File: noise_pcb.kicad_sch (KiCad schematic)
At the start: 29 parts, among them J101 PINK_OUT, J102 WHITE_OUT, J103 FILT_WHITE, J104 INV_FILT_WHITE, U1 TL072, U3 ElectricDruid_Noise2, U4 TL072

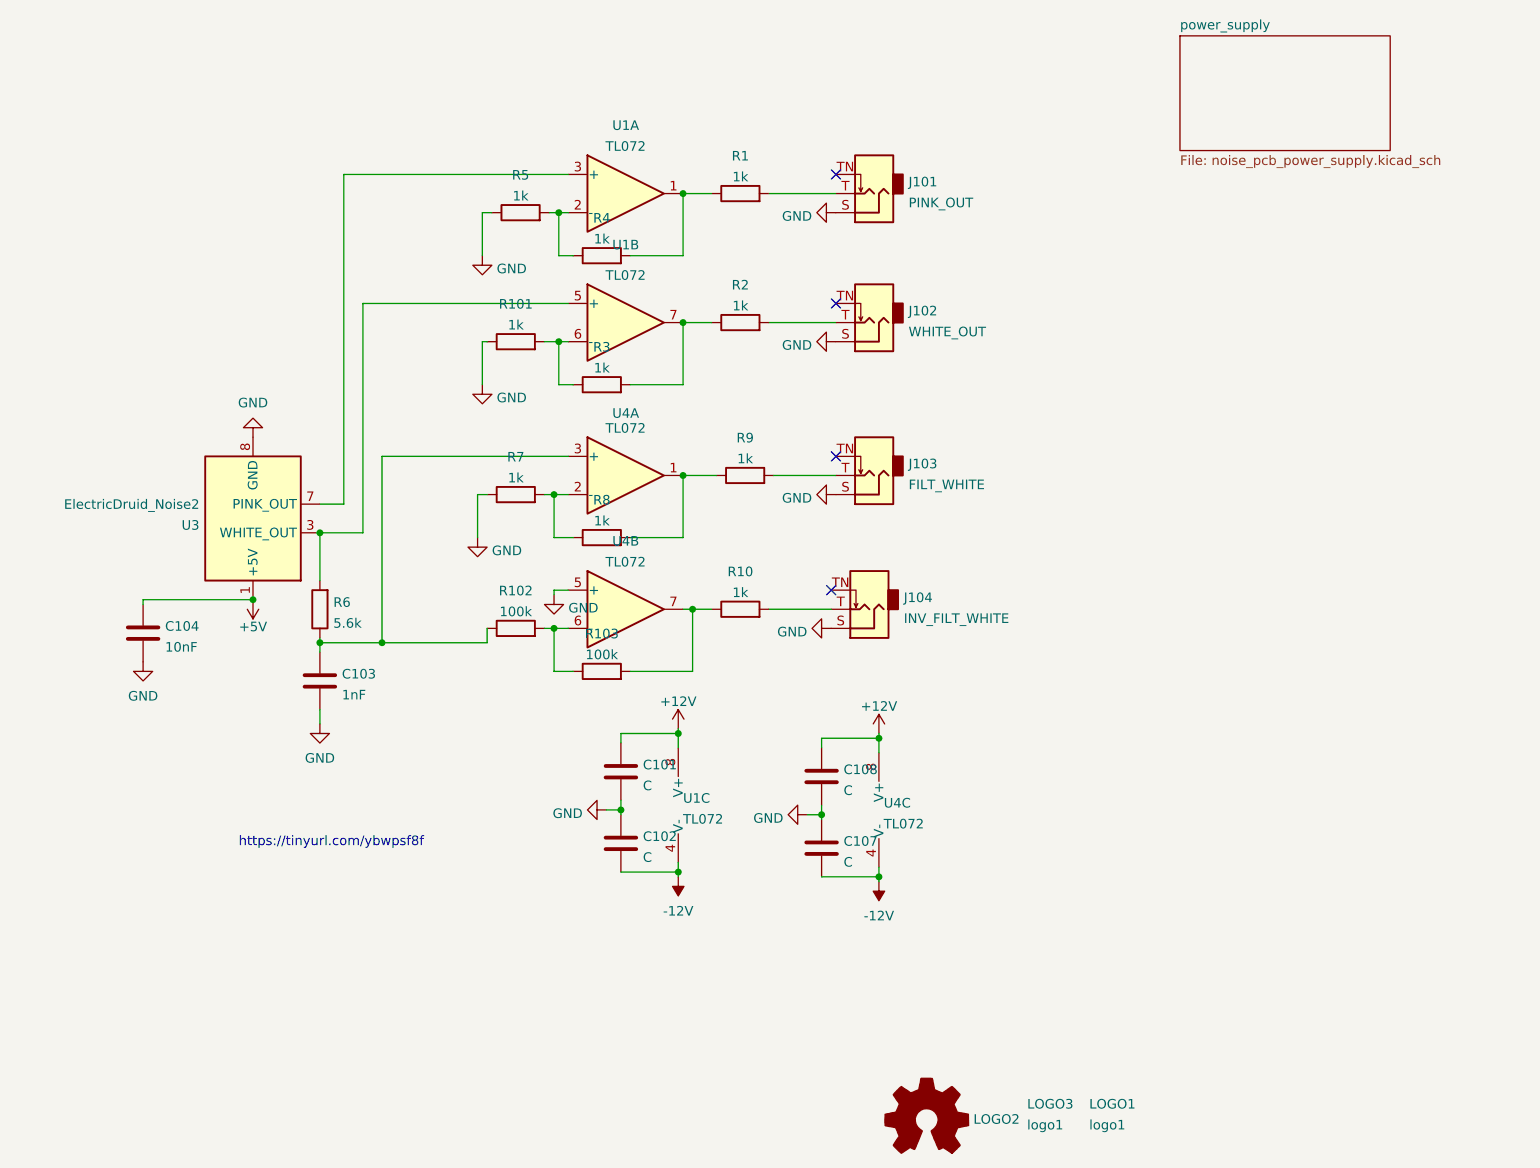
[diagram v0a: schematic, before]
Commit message: Assembly notes, value fixes, README
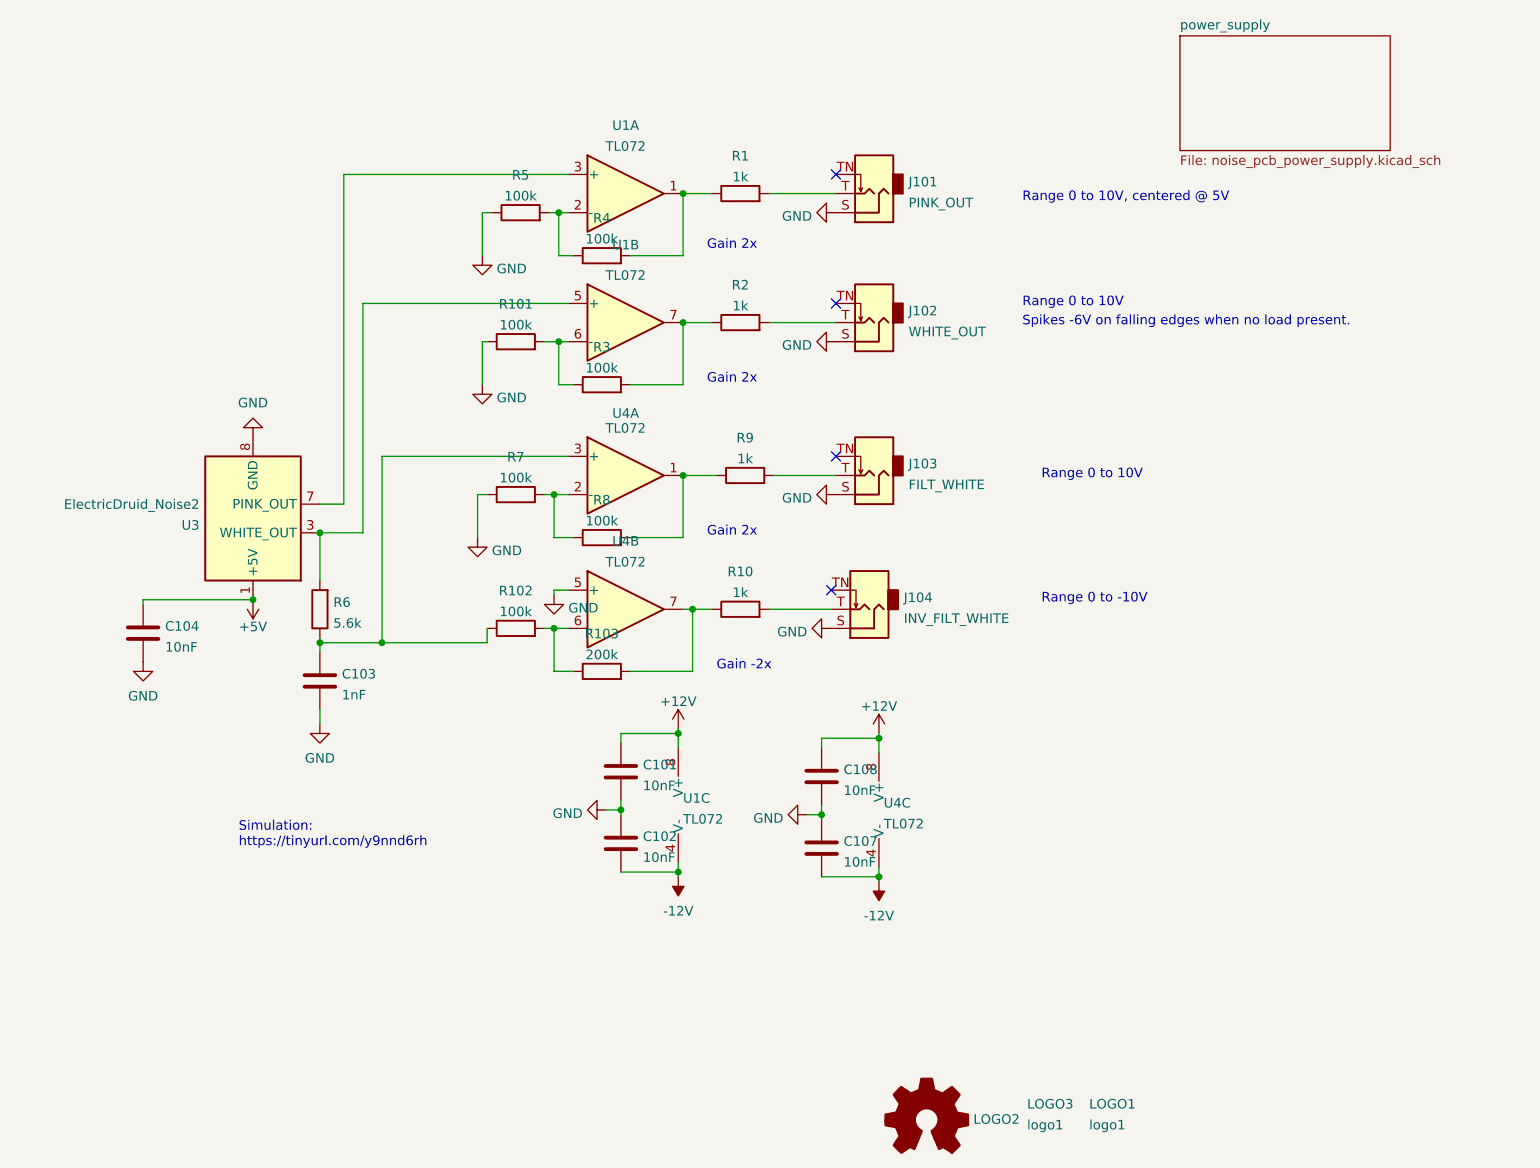
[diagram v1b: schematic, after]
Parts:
- C101, C102, C107, C108: value C -> 10nF
- R101, R3, R4, R5, R7, R8: value 1k -> 100k
- R103: value 100k -> 200k
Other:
- note added: "Gain -2x"
- note added: "Gain 2x"
- note added: "Range 0 to -10V"
- note added: "Range 0 to 10V"
- note added: "Range 0 to 10V, centered @ 5V"
- note added: "Simulation: https://tinyurl.com/y9nnd6rh"
- note added: "Spikes -6V on falling edges when no load present."
- note removed: "https://tinyurl.com/ybwpsf8f"
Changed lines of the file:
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@@
     (stroke (width 0) (type default) (color 0 0 0 0))
   )
-  (text "https://tinyurl.com/ybwpsf8f" (at 92.71 137.795 0)
+  (text "Gain -2x" (at 156.21 114.3 0)
+    (effects (font (size 1.27 1.27)) (justify left bottom))
+  )
+  (text "Range 0 to 10V, centered @ 5V" (at 196.85 52.07 0)
+    (effects (font (size 1.27 1.27)) (justify left bottom))
+  )
+  (text "Gain 2x" (at 154.94 76.2 0)
+    (effects (font (size 1.27 1.27)) (justify left bottom))
+  )
+  (text "Gain 2x" (at 154.94 58.42 0)
+    (effects (font (size 1.27 1.27)) (justify left bottom))
+  )
+  (text "Range 0 to 10V" (at 199.39 88.9 0)
+    (effects (font (size 1.27 1.27)) (justify left bottom))
+  )
+  (text "Simulation:\nhttps://tinyurl.com/y9nnd6rh" (at 92.71 137.795 0)
+    (effects (font (size 1.27 1.27)) (justify left bottom))
+  )
+  (text "Range 0 to -10V" (at 199.39 105.41 0)
+    (effects (font (size 1.27 1.27)) (justify left bottom))
+  )
+  (text "Spikes -6V on falling edges when no load present." (at 196.85 68.58 0)
+    (effects (font (size 1.27 1.27)) (justify left bottom))
+  )
+  (text "Range 0 to 10V" (at 196.85 66.04 0)
+    (effects (font (size 1.27 1.27)) (justify left bottom))
+  )
+  (text "Gain 2x" (at 154.94 96.52 0)
     (effects (font (size 1.27 1.27)) (justify left bottom))
   )
@@
       (effects (font (size 1.27 1.27)) (justify left))
     )
-    (property "Value" "C" (id 1) (at 173.101 139.6616 0)
+    (property "Value" "10nF" (id 1) (at 173.101 139.6616 0)
       (effects (font (size 1.27 1.27)) (justify left))
     )
@@
       (effects (font (size 1.27 1.27)) (justify left))
     )
-    (property "Value" "C" (id 1) (at 146.431 129.5016 0)
+    (property "Value" "10nF" (id 1) (at 146.431 129.5016 0)
       (effects (font (size 1.27 1.27)) (justify left))
     )
@@
       (effects (font (size 1.27 1.27)) (justify left))
     )
-    (property "Value" "C" (id 1) (at 146.431 139.0266 0)
+    (property "Value" "10nF" (id 1) (at 146.431 139.0266 0)
       (effects (font (size 1.27 1.27)) (justify left))
     )
@@
     (in_bom yes) (on_board yes) (fields_autoplaced)
     (property "Reference" "R4" (id 0) (at 140.97 54.0725 90))
-    (property "Value" "1k" (id 1) (at 140.97 56.8476 90))
+    (property "Value" "100k" (id 1) (at 140.97 56.8476 90))
     (property "Footprint" "Resistor_SMD:R_1206_3216Metric_Pad1.30x1.75mm_HandSolder" (id 2) (at 140.97 60.833 90)
       (effects (font (size 1.27 1.27)) hide)
@@
     (in_bom yes) (on_board yes) (fields_autoplaced)
     (property "Reference" "R5" (id 0) (at 130.175 48.3575 90))
-    (property "Value" "1k" (id 1) (at 130.175 51.1326 90))
+    (property "Value" "100k" (id 1) (at 130.175 51.1326 90))
     (property "Footprint" "Resistor_SMD:R_1206_3216Metric_Pad1.30x1.75mm_HandSolder" (id 2) (at 130.175 55.118 90)
       (effects (font (size 1.27 1.27)) hide)
@@
     (in_bom yes) (on_board yes)
     (property "Reference" "R8" (id 0) (at 140.97 91.5375 90))
-    (property "Value" "1k" (id 1) (at 140.97 94.3126 90))
+    (property "Value" "100k" (id 1) (at 140.97 94.3126 90))
     (property "Footprint" "Resistor_SMD:R_1206_3216Metric_Pad1.30x1.75mm_HandSolder" (id 2) (at 140.97 98.298 90)
       (effects (font (size 1.27 1.27)) hide)
@@
     (in_bom yes) (on_board yes) (fields_autoplaced)
     (property "Reference" "R101" (id 0) (at 129.54 65.5025 90))
-    (property "Value" "1k" (id 1) (at 129.54 68.2776 90))
+    (property "Value" "100k" (id 1) (at 129.54 68.2776 90))
     (property "Footprint" "Resistor_SMD:R_1206_3216Metric_Pad1.30x1.75mm_HandSolder" (id 2) (at 129.54 72.263 90)
       (effects (font (size 1.27 1.27)) hide)
@@
     (in_bom yes) (on_board yes) (fields_autoplaced)
     (property "Reference" "R7" (id 0) (at 129.54 85.8225 90))
-    (property "Value" "1k" (id 1) (at 129.54 88.5976 90))
+    (property "Value" "100k" (id 1) (at 129.54 88.5976 90))
     (property "Footprint" "Resistor_SMD:R_1206_3216Metric_Pad1.30x1.75mm_HandSolder" (id 2) (at 129.54 92.583 90)
       (effects (font (size 1.27 1.27)) hide)
@@
     (in_bom yes) (on_board yes) (fields_autoplaced)
     (property "Reference" "R3" (id 0) (at 140.97 71.2175 90))
-    (property "Value" "1k" (id 1) (at 140.97 73.9926 90))
+    (property "Value" "100k" (id 1) (at 140.97 73.9926 90))
     (property "Footprint" "Resistor_SMD:R_1206_3216Metric_Pad1.30x1.75mm_HandSolder" (id 2) (at 140.97 77.978 90)
       (effects (font (size 1.27 1.27)) hide)
@@
     (in_bom yes) (on_board yes)
     (property "Reference" "R103" (id 0) (at 140.97 109.3175 90))
-    (property "Value" "100k" (id 1) (at 140.97 112.0926 90))
+    (property "Value" "200k" (id 1) (at 140.97 112.0926 90))
     (property "Footprint" "Resistor_SMD:R_1206_3216Metric_Pad1.30x1.75mm_HandSolder" (id 2) (at 140.97 116.078 90)
       (effects (font (size 1.27 1.27)) hide)
@@
       (effects (font (size 1.27 1.27)) (justify left))
     )
-    (property "Value" "C" (id 1) (at 173.101 130.1366 0)
+    (property "Value" "10nF" (id 1) (at 173.101 130.1366 0)
       (effects (font (size 1.27 1.27)) (justify left))
     )
@@
     )
     (path "/6a71deaf-8ed8-4b4e-a097-04761c3a9b7b"
-      (reference "C101") (unit 1) (value "C") (footprint "Capacitor_THT:C_Disc_D6.0mm_W4.4mm_P5.00mm")
+      (reference "C101") (unit 1) (value "10nF") (footprint "Capacitor_THT:C_Disc_D6.0mm_W4.4mm_P5.00mm")
     )
     (path "/6b96e9a1-e255-499a-aa20-f60ecd5d6955"
-      (reference "C102") (unit 1) (value "C") (footprint "Capacitor_THT:C_Disc_D6.0mm_W4.4mm_P5.00mm")
+      (reference "C102") (unit 1) (value "10nF") (footprint "Capacitor_THT:C_Disc_D6.0mm_W4.4mm_P5.00mm")
     )
     (path "/8f5ce17a-fae1-470f-a98d-221b0e94565d"
@@
     )
     (path "/2ed1b884-98f0-400f-97e6-6e1445d7a0b8"
-      (reference "C107") (unit 1) (value "C") (footprint "Capacitor_THT:C_Disc_D6.0mm_W4.4mm_P5.00mm")
+      (reference "C107") (unit 1) (value "10nF") (footprint "Capacitor_THT:C_Disc_D6.0mm_W4.4mm_P5.00mm")
     )
     (path "/ffb095dd-5623-4b48-97b7-581bd252c9b2"
-      (reference "C108") (unit 1) (value "C") (footprint "Capacitor_THT:C_Disc_D6.0mm_W4.4mm_P5.00mm")
+      (reference "C108") (unit 1) (value "10nF") (footprint "Capacitor_THT:C_Disc_D6.0mm_W4.4mm_P5.00mm")
     )
     (path "/c045b4c2-7302-48c5-b137-d1ad353be048/05c022a7-f9f5-45a3-9346-213e8fce81d3"
@@
     )
     (path "/ae4abfc0-c74f-4aca-ac2d-a9ea6aacaaaf"
-      (reference "R3") (unit 1) (value "1k") (footprint "Resistor_SMD:R_1206_3216Metric_Pad1.30x1.75mm_HandSolder")
+      (reference "R3") (unit 1) (value "100k") (footprint "Resistor_SMD:R_1206_3216Metric_Pad1.30x1.75mm_HandSolder")
     )
     (path "/796365eb-3b00-481a-b3b0-b83241f40275"
-      (reference "R4") (unit 1) (value "1k") (footprint "Resistor_SMD:R_1206_3216Metric_Pad1.30x1.75mm_HandSolder")
+      (reference "R4") (unit 1) (value "100k") (footprint "Resistor_SMD:R_1206_3216Metric_Pad1.30x1.75mm_HandSolder")
     )
     (path "/8134c256-d4c7-4a69-b994-3108ed996f95"
-      (reference "R5") (unit 1) (value "1k") (footprint "Resistor_SMD:R_1206_3216Metric_Pad1.30x1.75mm_HandSolder")
+      (reference "R5") (unit 1) (value "100k") (footprint "Resistor_SMD:R_1206_3216Metric_Pad1.30x1.75mm_HandSolder")
     )
     (path "/0bee5d4c-0b61-4267-a49e-f88f005cf8b6"
@@
     )
     (path "/abd560d3-acc2-4742-b462-be0765f942b5"
-      (reference "R7") (unit 1) (value "1k") (footprint "Resistor_SMD:R_1206_3216Metric_Pad1.30x1.75mm_HandSolder")
+      (reference "R7") (unit 1) (value "100k") (footprint "Resistor_SMD:R_1206_3216Metric_Pad1.30x1.75mm_HandSolder")
     )
     (path "/8adab083-05b5-4a52-9cab-e1546510f4c1"
-      (reference "R8") (unit 1) (value "1k") (footprint "Resistor_SMD:R_1206_3216Metric_Pad1.30x1.75mm_HandSolder")
+      (reference "R8") (unit 1) (value "100k") (footprint "Resistor_SMD:R_1206_3216Metric_Pad1.30x1.75mm_HandSolder")
     )
     (path "/6b55610a-a6bb-470f-b556-b39436ab4bbf"
@@
     )
     (path "/8fd95ddc-a582-497f-8905-973e937da1a0"
-      (reference "R101") (unit 1) (value "1k") (footprint "Resistor_SMD:R_1206_3216Metric_Pad1.30x1.75mm_HandSolder")
+      (reference "R101") (unit 1) (value "100k") (footprint "Resistor_SMD:R_1206_3216Metric_Pad1.30x1.75mm_HandSolder")
     )
     (path "/f4aefe93-5b2d-431f-8bb1-6afb22325813"
@@
     )
     (path "/ef7ff756-d2a6-4ae0-8373-5dceb07e0d02"
-      (reference "R103") (unit 1) (value "100k") (footprint "Resistor_SMD:R_1206_3216Metric_Pad1.30x1.75mm_HandSolder")
+      (reference "R103") (unit 1) (value "200k") (footprint "Resistor_SMD:R_1206_3216Metric_Pad1.30x1.75mm_HandSolder")
     )
     (path "/2b3b289c-9356-4727-acba-91ef9abb00ec"

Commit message: Title block updates and pdf
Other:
- company: (none) -> Robot Dialogs
- title: noise_pcb -> Noise PCB
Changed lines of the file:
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@@
   (paper "A4")
   (title_block
-    (title "noise_pcb")
+    (title "Noise PCB")
     (date "2022-01-31")
-    (rev "v1")
+    (rev "1.0")
+    (company "Robot Dialogs")
   )
   (junction (at 134.62 108.585) (diameter 0) (color 0 0 0 0)
@@
     (pin "1")
   )
-  (symbol (lib_id "My Stuff:logo1") (at 205.105 172.72 0) (unit 1)
-    (in_bom yes) (on_board yes) (fields_autoplaced)
-    (property "Reference" "LOGO1" (id 0) (at 205.74 171.8115 0)
-      (effects (font (size 1.27 1.27)) (justify left))
-    )
-    (property "Value" "logo1" (id 1) (at 205.74 174.5866 0)
-      (effects (font (size 1.27 1.27)) (justify left))
-    )
-    (property "Footprint" "My Stuff:Logo2" (id 2) (at 205.105 171.45 0)
-      (effects (font (size 1.27 1.27)) hide)
-    )
-    (property "Datasheet" "" (id 3) (at 205.105 171.45 0)
+  (symbol (lib_id "My Stuff:logo1") (at 220.98 172.085 0) (unit 1)
+    (in_bom yes) (on_board yes) (fields_autoplaced)
+    (property "Reference" "LOGO1" (id 0) (at 221.615 171.1765 0)
+      (effects (font (size 1.27 1.27)) (justify left))
+    )
+    (property "Value" "logo1" (id 1) (at 221.615 173.9516 0)
+      (effects (font (size 1.27 1.27)) (justify left))
+    )
+    (property "Footprint" "My Stuff:Logo2" (id 2) (at 220.98 170.815 0)
+      (effects (font (size 1.27 1.27)) hide)
+    )
+    (property "Datasheet" "" (id 3) (at 220.98 170.815 0)
       (effects (font (size 1.27 1.27)) hide)
     )
@@
     (pin "2")
   )
-  (symbol (lib_id "My Stuff:logo1") (at 196.85 172.72 0) (unit 1)
-    (in_bom yes) (on_board yes) (fields_autoplaced)
-    (property "Reference" "LOGO3" (id 0) (at 197.485 171.8115 0)
-      (effects (font (size 1.27 1.27)) (justify left))
-    )
-    (property "Value" "logo1" (id 1) (at 197.485 174.5866 0)
-      (effects (font (size 1.27 1.27)) (justify left))
-    )
-    (property "Footprint" "My Stuff:Logo1" (id 2) (at 196.85 171.45 0)
-      (effects (font (size 1.27 1.27)) hide)
-    )
-    (property "Datasheet" "" (id 3) (at 196.85 171.45 0)
-      (effects (font (size 1.27 1.27)) hide)
-    )
+  (symbol (lib_id "My Stuff:logo1") (at 204.47 172.085 0) (unit 1)
+    (in_bom yes) (on_board yes) (fields_autoplaced)
+    (property "Reference" "LOGO3" (id 0) (at 205.105 171.1765 0)
+      (effects (font (size 1.27 1.27)) (justify left))
+    )
+    (property "Value" "logo1" (id 1) (at 205.105 173.9516 0)
+      (effects (font (size 1.27 1.27)) (justify left))
+    )
+    (property "Footprint" "My Stuff:Logo1" (id 2) (at 204.47 170.815 0)
+      (effects (font (size 1.27 1.27)) hide)
+    )
+    (property "Datasheet" "" (id 3) (at 204.47 170.815 0)
+      (effects (font (size 1.27 1.27)) hide)
+    )
